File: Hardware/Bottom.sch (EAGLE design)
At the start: 91 parts, among them IC1 SI570, IC2 74LVC74A, IC3 74LVC1G17DCK, IC5 LT6232CGN, Q1 DMPH6050SK3

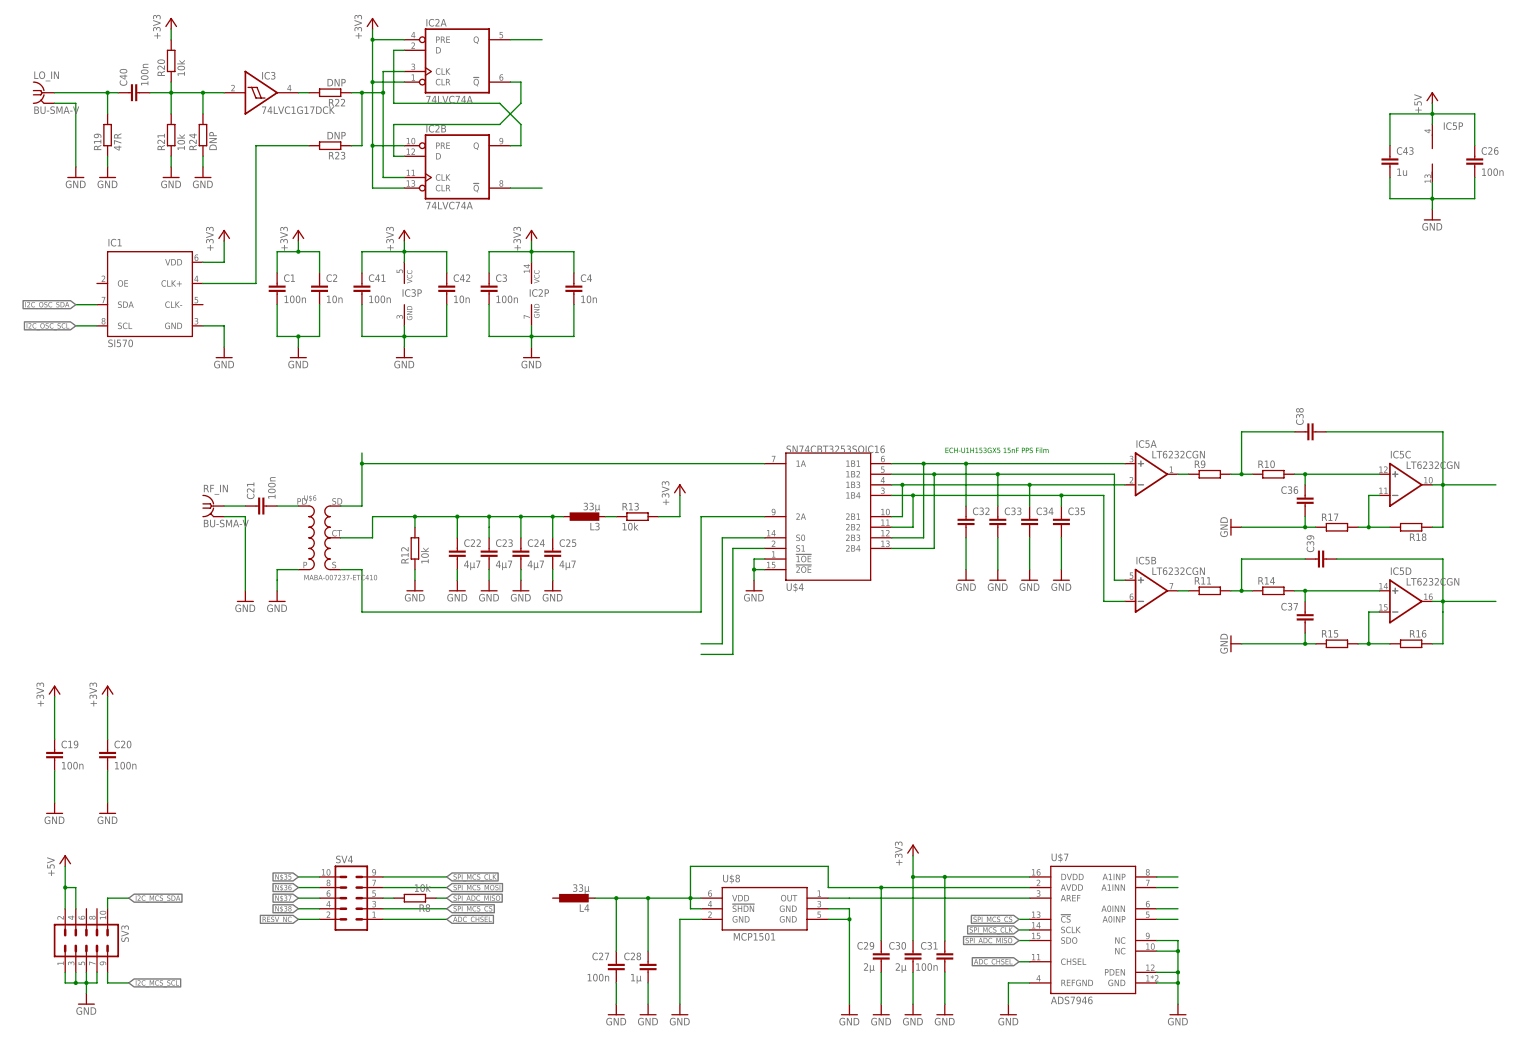
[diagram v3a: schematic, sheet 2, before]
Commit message: Advance layout bottom
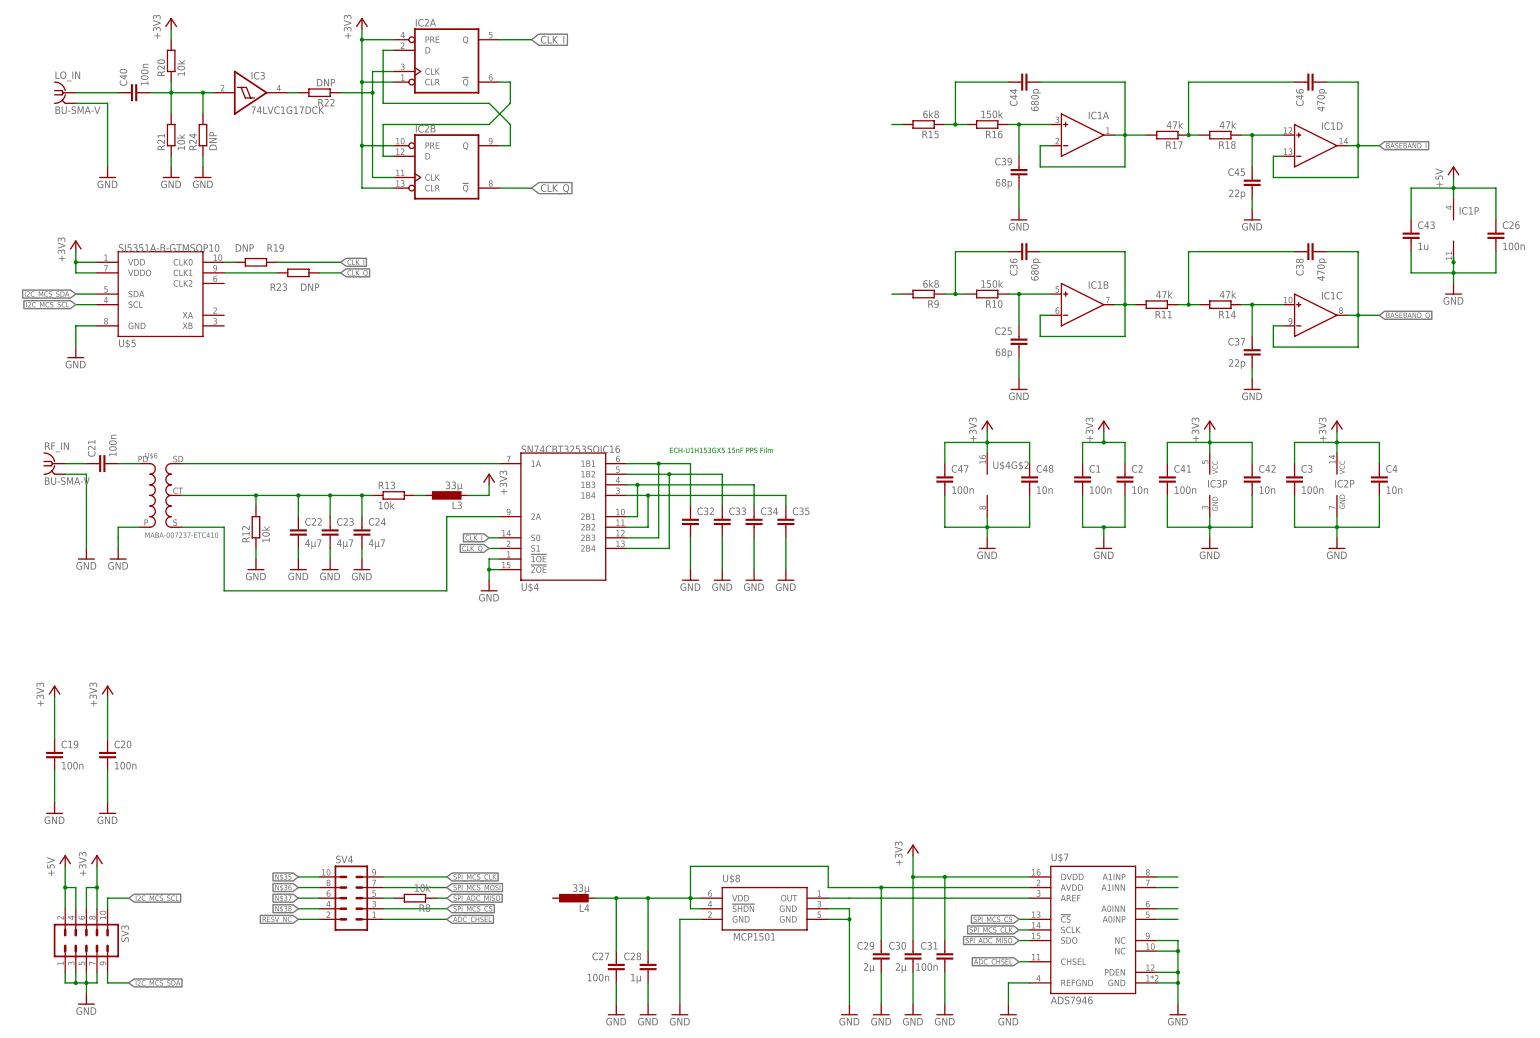
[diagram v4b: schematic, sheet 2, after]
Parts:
- removed IC5: LT6232CGN, linear-technology:LT6232CGN
- added C44: 680p, rcl:C-EUC0603
- added C45: 22p, rcl:C-EUC0603
- added C46: 470p, rcl:C-EUC0603
- added C47: 100n, rcl:C-EUC0402
- added C48: 10n, rcl:C-EUC0402
- added U$5: SI5351A-B-GTMSOP10, MyLib:SI5351A-B-GTMSOP10
- C24: device rcl:C-EUC0805 -> rcl:C-EUC0402
- C25: value 4µ7 -> 68p; device rcl:C-EUC0805 -> rcl:C-EUC0603
- C32, C33, C34, C35: device rcl:C-EUC1210 -> rcl:C-EUC1206
- C36: value (none) -> 680p
- C37: value (none) -> 22p
- C38: value (none) -> 470p
- C39: value (none) -> 68p
- IC1: value SI570 -> OP491SOIC_N14; device silabs:SI570 -> MyLib:OP491SOIC_N14
- IC2: value 74LVC74A -> 74AC74D
- R10, R16: value (none) -> 150k
- R11, R14, R17, R18: value (none) -> 47k
- R15, R9: value (none) -> 6k8
- R19: value 47R -> DNP
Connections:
- removed net I2C_OSC_SCL: IC1.SCL
- removed net I2C_OSC_SDA: IC1.SDA
- removed net N$22: U$4G$1.S1
- removed net N$40: C38.1, R10.1, R9.2
- removed net N$45: IC5C.-IN, R17.2, R18.2
- removed net N$59: C34.1, IC5A.-IN, U$4G$1.1B3, U$4G$1.2B1
- new net BASEBAND_I: C46.2, IC1D.IN-, IC1D.OUT
- new net BASEBAND_Q: C38.2, IC1C.IN-, IC1C.OUT
- new net CLK_I: IC2A.Q, R19.1, U$4G$1.S0
- new net CLK_Q: IC2B.!Q, R23.1, U$4G$1.S1
- new net N$34: C35.1, U$4G$1.1B4, U$4G$1.2B2
- new net N$53: C33.1, U$4G$1.1B2, U$4G$1.2B4
- new net N$54: C45.1, IC1D.IN+, R18.1
- net +3V3: now also C47.1, C48.1, L3.2, SV3.6, SV3.8, U$4G$2.V+, U$5.VDD, U$5.VDDO; no longer IC1.VDD, R13.2
- net +5V: now also IC1P.V+; no longer IC5P.V+
- net GND: now also C39.2, C45.2, C47.2, C48.2, IC1P.V-, U$4G$2.V-, U$5.GND; no longer C36.2, IC1.GND, IC5P.V-, R15.1, R17.1, R19.1
- net I2C_MCS_SCL: now also SV3.10, U$5.SCL; no longer SV3.9
- net I2C_MCS_SDA: now also SV3.9, U$5.SDA; no longer SV3.10
- net N$1: now also R19.2, U$5.CLK0; no longer IC2A.Q
- net N$10: now also C36.1, R10.2, R9.1; no longer C39.1, R11.2, R14.1
- net N$13: now also C25.1, IC1B.IN+, R10.1; no longer C37.1, IC5D.+IN, R14.2
- net N$14: now also C36.2, IC1B.IN-, IC1B.OUT, R11.2; no longer IC5A.OUT, R9.1
- net N$18: now also R13.1; no longer C25.1, L3.1
- net N$2: no longer R23.1
- net N$21: now also L3.1, R13.2; no longer L3.2, R13.1
- net N$23: now also C34.1, U$4G$1.1B3, U$4G$1.2B1; no longer U$4G$1.S0
- net N$24: no longer IC5A.+IN
- net N$33: now also C38.1, R11.1, R14.2; no longer C33.1, IC5B.+IN, U$4G$1.1B2, U$4G$1.2B4
- net N$39: now also C37.1, IC1C.IN+, R14.1; no longer C35.1, IC5B.-IN, U$4G$1.1B4, U$4G$1.2B2
- net N$41: now also R15.2; no longer C36.1, IC5C.+IN, R10.2
- net N$42: now also C44.1, R15.1, R16.2; no longer C38.2, IC5C.OUT, R18.1
- net N$43: now also C39.1, IC1A.IN+; no longer C39.2, IC5D.OUT
- net N$44: now also C44.2, IC1A.IN-, IC1A.OUT, R17.2; no longer IC5D.-IN, R15.2, R16.2
- net N$46: no longer R19.2
- net N$5: now also R23.2, U$5.CLK1; no longer IC2B.!Q
- net N$50: now also C46.1, R17.1, R18.2; no longer IC1.CLK+, R23.2
- net N$6: now also R9.2; no longer IC5B.OUT, R11.1
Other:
- moved on the sheet: C1, C2, C21, C22, C23, C24, C25, C26, C3, C32, C33, C34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

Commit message: Add RF Buffer
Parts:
- removed U$4: SN74CBT3253SOIC16, MyLib:SN74CBT3253SOIC16
- added C49: 100n, rcl:C-EUC0402
- added C50: 10n, rcl:C-EUC0402
- added IC4: LT6231, MyLib:LT6231
- added IC5: SN74CBT3253SOIC16, MyLib:SN74CBT3253SOIC16
- added Q2: 25MHz, MyLib:ABM10W-25.0000MHZ-6-B1U-T3
- added R25, R26, R27, R28, R29, R30: 100R, rcl:R-EU_R0603
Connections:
- new net N$22: IC4B.IN+, R25.1
- new net N$40: IC4B.IN-, R26.1, R29.2
- new net N$45: IC4A.IN+, R27.1
- new net N$55: IC4A.IN-, R28.1, R30.2
- new net N$56: Q2.2, U$5.XA
- new net N$57: IC4B.OUT, R15.2, R29.1
- net +3V3: now also C26.1, C43.1, C49.1, C50.1, IC1P.V+, IC4P.V+, IC5P.V+; no longer U$4G$2.V+
- net +5V: no longer C26.1, C43.1, IC1P.V+
- net CLK_I: now also IC5A.S0; no longer U$4G$1.S0
- net CLK_Q: now also IC5A.S1; no longer U$4G$1.S1
- net GND: now also C49.2, C50.2, IC4P.V-, IC5A.!1OE, IC5A.!2OE, IC5P.V-; no longer U$4G$1.!1OE, U$4G$1.!2OE, U$4G$2.V-
- net N$23: now also IC5A.1B3, IC5A.2B1, R27.2; no longer U$4G$1.1B3, U$4G$1.2B1
- net N$24: now also IC5A.1B1, IC5A.2B3, R25.2; no longer U$4G$1.1B1, U$4G$1.2B3
- net N$34: now also IC5A.1B4, IC5A.2B2, R28.2; no longer U$4G$1.1B4, U$4G$1.2B2
- net N$41: now also Q2.1, U$5.XB; no longer R15.2
- net N$51: now also IC5A.2A; no longer U$4G$1.2A
- net N$52: now also IC5A.1A; no longer U$4G$1.1A
- net N$53: now also IC5A.1B2, IC5A.2B4, R26.2; no longer U$4G$1.1B2, U$4G$1.2B4
- net N$6: now also IC4A.OUT, R30.1
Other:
- moved on the sheet: C1, C2, C25, C26, C3, C36, C37, C38, C39, C4, C41, C42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

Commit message: Add various parts
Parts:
- added BB_I, BB_Q: BU-SMA-V, con-coax:BU-SMA-V
- added JP3: (no value), pinhead:PINHD-2X3
- added R31, R32: DNP, rcl:R-EU_R0603
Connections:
- removed net N$25: U$7.A1INP
- removed net N$28: U$7.A0INN
- new net N$58: IC2B.!Q, R32.2
- new net N$59: IC2A.Q, R31.2
- net BASEBAND_I: now also BB_I.1, JP3.2
- net BASEBAND_Q: now also BB_Q.1, JP3.6
- net CLK_I: now also R31.1; no longer IC2A.Q
- net CLK_Q: now also R32.1; no longer IC2B.!Q
- net GND: now also BB_I.2, BB_Q.2, JP3.3, JP3.4, U$7.A0INN, U$7.A1INN
- net N$26: now also JP3.1, U$7.A1INP; no longer U$7.A1INN
- net N$32: now also JP3.5

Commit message: Add various parts
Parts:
- removed C42: 10n, rcl:C-EUC0402
- removed C43: 1u, rcl:C-EUC0603
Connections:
- net +3V3: no longer C42.1, C43.1
- net GND: no longer C42.2, C43.2
- net I2C_MCS_SCL: now also SV3.9; no longer SV3.10
- net I2C_MCS_SDA: now also SV3.10; no longer SV3.9
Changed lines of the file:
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@@
 <part name="+3V11" library="supply1" library_urn="urn:adsk.eagle:library:371" deviceset="+3V3" device=""/>
 <part name="C41" library="rcl" library_urn="urn:adsk.eagle:library:334" deviceset="C-EU" device="C0402" package3d_urn="urn:adsk.eagle:package:23626/1" value="100n"/>
-<part name="C42" library="rcl" library_urn="urn:adsk.eagle:library:334" deviceset="C-EU" device="C0402" package3d_urn="urn:adsk.eagle:package:23626/1" value="10n"/>
 <part name="GND55" library="supply1" library_urn="urn:adsk.eagle:library:371" deviceset="GND" device=""/>
 <part name="+3V12" library="supply1" library_urn="urn:adsk.eagle:library:371" deviceset="+3V3" device=""/>
-<part name="C43" library="rcl" library_urn="urn:adsk.eagle:library:334" deviceset="C-EU" device="C0603" package3d_urn="urn:adsk.eagle:package:23616/2" value="1u"/>
 <part name="RF_IN" library="con-coax" library_urn="urn:adsk.eagle:library:133" deviceset="BU-SMA-V" device="" package3d_urn="urn:adsk.eagle:package:6211/1"/>
 <part name="LO_IN" library="con-coax" library_urn="urn:adsk.eagle:library:133" deviceset="BU-SMA-V" device="" package3d_urn="urn:adsk.eagle:package:6211/1"/>
@@
 <attribute name="VALUE" x="359.664" y="236.601" size="1.778" layer="96"/>
 </instance>
-<instance part="C42" gate="G$1" x="378.46" y="241.3" smashed="yes">
-<attribute name="NAME" x="379.984" y="241.681" size="1.778" layer="95"/>
-<attribute name="VALUE" x="379.984" y="236.601" size="1.778" layer="96"/>
-</instance>
 <instance part="GND55" gate="1" x="368.3" y="223.52" smashed="yes">
 <attribute name="VALUE" x="365.76" y="220.98" size="1.778" layer="96"/>
@@
 <instance part="+3V12" gate="G$1" x="368.3" y="254" smashed="yes">
 <attribute name="VALUE" x="365.76" y="248.92" size="1.778" layer="96" rot="R90"/>
-</instance>
-<instance part="C43" gate="G$1" x="292.1" y="241.3" smashed="yes">
-<attribute name="NAME" x="293.624" y="241.681" size="1.778" layer="95"/>
-<attribute name="VALUE" x="293.624" y="236.601" size="1.778" layer="96"/>
 </instance>
 <instance part="RF_IN" gate="G$1" x="15.24" y="142.24" smashed="yes">
@@
 <wire x1="312.42" y1="228.6" x2="302.26" y2="228.6" width="0.1524" layer="91"/>
 <junction x="302.26" y="228.6"/>
-<pinref part="C43" gate="G$1" pin="2"/>
-<wire x1="292.1" y1="236.22" x2="292.1" y2="228.6" width="0.1524" layer="91"/>
-<wire x1="292.1" y1="228.6" x2="302.26" y2="228.6" width="0.1524" layer="91"/>
 <pinref part="IC1" gate="P" pin="V-"/>
 <junction x="302.26" y="231.14"/>
@@
 <pinref part="GND55" gate="1" pin="GND"/>
 <wire x1="368.3" y1="228.6" x2="368.3" y2="226.06" width="0.1524" layer="91"/>
-<wire x1="368.3" y1="228.6" x2="378.46" y2="228.6" width="0.1524" layer="91"/>
 <junction x="368.3" y="228.6"/>
-<pinref part="C42" gate="G$1" pin="2"/>
-<wire x1="378.46" y1="228.6" x2="378.46" y2="236.22" width="0.1524" layer="91"/>
 <wire x1="368.3" y1="231.14" x2="368.3" y2="228.6" width="0.1524" layer="91"/>
 <pinref part="IC3" gate="P" pin="GND"/>
@@
 <pinref part="+3V12" gate="G$1" pin="+3V3"/>
 <wire x1="368.3" y1="248.92" x2="368.3" y2="251.46" width="0.1524" layer="91"/>
-<wire x1="368.3" y1="248.92" x2="378.46" y2="248.92" width="0.1524" layer="91"/>
 <junction x="368.3" y="248.92"/>
-<pinref part="C42" gate="G$1" pin="1"/>
-<wire x1="378.46" y1="248.92" x2="378.46" y2="243.84" width="0.1524" layer="91"/>
 <wire x1="368.3" y1="246.38" x2="368.3" y2="248.92" width="0.1524" layer="91"/>
 <pinref part="IC3" gate="P" pin="VCC"/>
@@
 <pinref part="C26" gate="G$1" pin="1"/>
 <wire x1="312.42" y1="248.92" x2="312.42" y2="243.84" width="0.1524" layer="91"/>
-<wire x1="302.26" y1="248.92" x2="292.1" y2="248.92" width="0.1524" layer="91"/>
-<pinref part="C43" gate="G$1" pin="1"/>
-<wire x1="292.1" y1="248.92" x2="292.1" y2="243.84" width="0.1524" layer="91"/>
 <pinref part="IC1" gate="P" pin="V+"/>
 <pinref part="+3V13" gate="G$1" pin="+3V3"/>
@@
 <net name="I2C_MCS_SDA" class="0">
 <segment>
+<wire x1="167.64" y1="236.22" x2="162.56" y2="236.22" width="0.1524" layer="91"/>
+<label x="162.56" y="236.22" size="1.27" layer="95" rot="R180" xref="yes"/>
+<pinref part="U$5" gate="G$1" pin="SDA"/>
+</segment>
+<segment>
+<wire x1="27.94" y1="38.1" x2="33.02" y2="38.1" width="0.1524" layer="91"/>
+<label x="33.02" y="38.1" size="1.27" layer="95" xref="yes"/>
+<pinref part="SV3" gate="G$1" pin="10"/>
+<wire x1="27.94" y1="35.56" x2="27.94" y2="38.1" width="0.1524" layer="91"/>
+</segment>
+</net>
+<net name="I2C_MCS_SCL" class="0">
+<segment>
+<wire x1="167.64" y1="233.68" x2="162.56" y2="233.68" width="0.1524" layer="91"/>
+<label x="162.56" y="233.68" size="1.27" layer="95" rot="R180" xref="yes"/>
+<pinref part="U$5" gate="G$1" pin="SCL"/>
+</segment>
+<segment>
 <wire x1="27.94" y1="17.78" x2="33.02" y2="17.78" width="0.1524" layer="91"/>
 <label x="33.02" y="17.78" size="1.27" layer="95" xref="yes"/>
@@
 <wire x1="27.94" y1="20.32" x2="27.94" y2="17.78" width="0.1524" layer="91"/>
 </segment>
-<segment>
-<wire x1="167.64" y1="236.22" x2="162.56" y2="236.22" width="0.1524" layer="91"/>
-<label x="162.56" y="236.22" size="1.27" layer="95" rot="R180" xref="yes"/>
-<pinref part="U$5" gate="G$1" pin="SDA"/>
-</segment>
-</net>
-<net name="I2C_MCS_SCL" class="0">
-<segment>
-<wire x1="27.94" y1="38.1" x2="33.02" y2="38.1" width="0.1524" layer="91"/>
-<label x="33.02" y="38.1" size="1.27" layer="95" xref="yes"/>
-<pinref part="SV3" gate="G$1" pin="10"/>
-<wire x1="27.94" y1="35.56" x2="27.94" y2="38.1" width="0.1524" layer="91"/>
-</segment>
-<segment>
-<wire x1="167.64" y1="233.68" x2="162.56" y2="233.68" width="0.1524" layer="91"/>
-<label x="162.56" y="233.68" size="1.27" layer="95" rot="R180" xref="yes"/>
-<pinref part="U$5" gate="G$1" pin="SCL"/>
-</segment>
-</net>
+</net>
